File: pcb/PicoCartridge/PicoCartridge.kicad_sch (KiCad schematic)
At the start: 0 parts

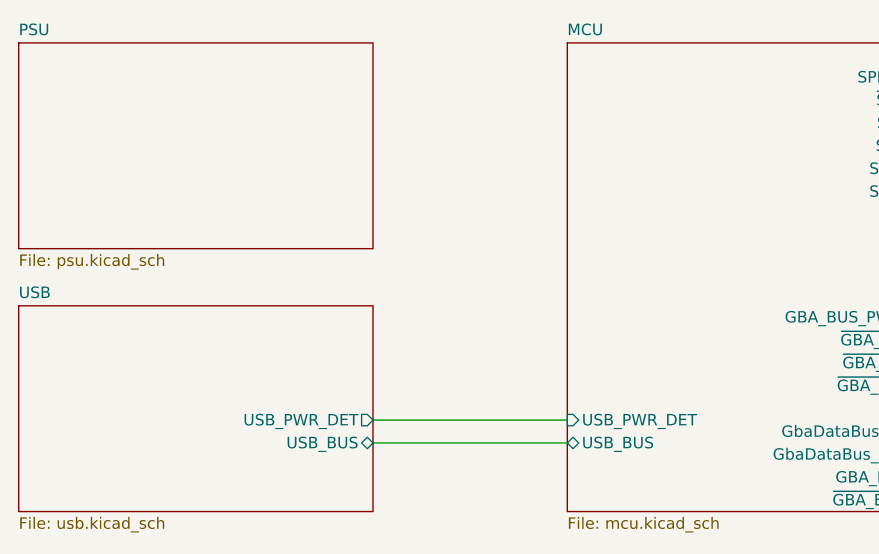
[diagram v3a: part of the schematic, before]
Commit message: Added programmer connection (#4)
* Removed dedicated usb connector

Use would be very limited (live view on a pc and data transfer without
removing the sd card) and increases the pcb & schematic complexity by a lot.

Removing the usb connector for this revision. It is possible, if this design
is successful that I will create a new revision at some point. You never know.

* Added programmer "connector"

Additionally removed reset and program switches as there is no need for
them on the pcb itself if there is no usb connection.
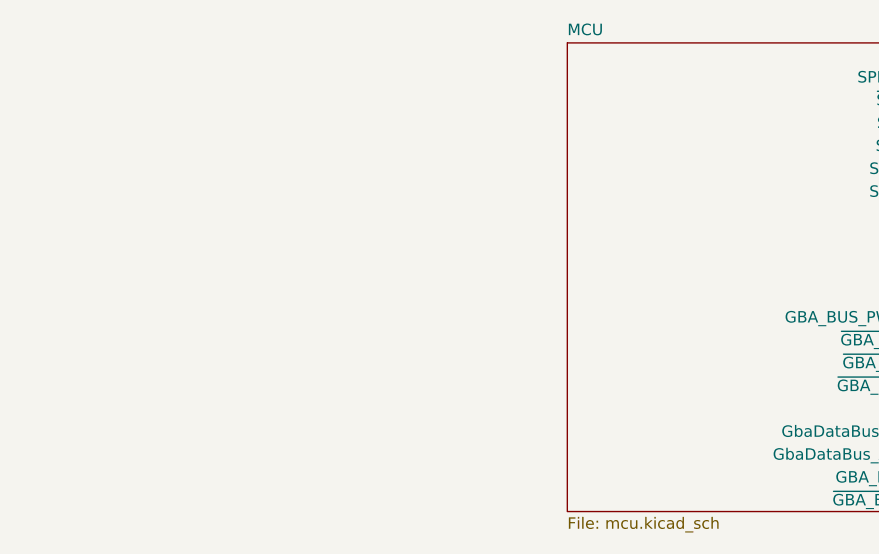
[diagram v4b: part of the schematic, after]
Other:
- removed sheet PSU
- removed sheet USB
- sheet MCU ports: added none; removed USB_BUS, USB_PWR_DET
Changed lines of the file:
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@@
-		)
-	)
-	(wire
-		(pts
-			(xy 73.66 69.85) (xy 95.25 69.85)
-		)
-		(stroke
-			(width 0)
-			(type default)
 		)
 	)
@@
 	(wire
 		(pts
-			(xy 73.66 67.31) (xy 95.25 67.31)
-		)
-		(stroke
-			(width 0)
-			(type default)
-		)
-	)
-	(wire
-		(pts
 			(xy 138.43 76.2) (xy 156.21 76.2)
 		)
@@
 			(width 0)
 			(type default)
-		)
-	)
-	(sheet
-		(at 34.29 25.4)
-		(size 39.37 22.86)
-		(fields_autoplaced yes)
-		(stroke
-			(width 0.1524)
-			(type solid)
-		)
-		(fill
-			(color 0 0 0 0.0000)
-		)
-		(property "Sheetname" "PSU"
-			(at 34.29 24.6884 0)
-			(effects
-				(font
-					(size 1.27 1.27)
-				)
-				(justify left bottom)
-			)
-		)
-		(property "Sheetfile" "psu.kicad_sch"
-			(at 34.29 48.8446 0)
-			(effects
-				(font
-					(size 1.27 1.27)
-				)
-				(justify left top)
-			)
-		)
-		(instances
-			(project "PicoCartridge"
-				(path "/369b8492-ac84-4ba1-9646-4010d0ed9f44"
-					(page "3")
-				)
-			)
 		)
 	)
@@
 	)
 	(sheet
-		(at 34.29 54.61)
-		(size 39.37 22.86)
-		(fields_autoplaced yes)
-		(stroke
-			(width 0.1524)
-			(type solid)
-		)
-		(fill
-			(color 0 0 0 0.0000)
-		)
-		(property "Sheetname" "USB"
-			(at 34.29 53.8984 0)
-			(effects
-				(font
-					(size 1.27 1.27)
-				)
-				(justify left bottom)
-			)
-		)
-		(property "Sheetfile" "usb.kicad_sch"
-			(at 34.29 78.0546 0)
-			(effects
-				(font
-					(size 1.27 1.27)
-				)
-				(justify left top)
-			)
-		)
-		(pin "USB_BUS" bidirectional
-			(at 73.66 69.85 0)
-			(effects
-				(font
-					(size 1.27 1.27)
-				)
-				(justify right)
-			)
-		)
-		(pin "USB_PWR_DET" output
-			(at 73.66 67.31 0)
-			(effects
-				(font
-					(size 1.27 1.27)
-				)
-				(justify right)
-			)
-		)
-		(instances
-			(project "PicoCartridge"
-				(path "/369b8492-ac84-4ba1-9646-4010d0ed9f44"
-					(page "6")
-				)
-			)
-		)
-	)
-	(sheet
 		(at 156.21 25.4)
 		(size 39.37 22.86)
@@
 			)
 		)
-		(pin "USB_PWR_DET" input
-			(at 95.25 67.31 180)
-			(effects
-				(font
-					(size 1.27 1.27)
-				)
-				(justify left)
-			)
-		)
-		(pin "USB_BUS" bidirectional
-			(at 95.25 69.85 180)
-			(effects
-				(font
-					(size 1.27 1.27)
-				)
-				(justify left)
-			)
-		)
